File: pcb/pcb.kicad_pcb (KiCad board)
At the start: 2 copper layers, 99.9 x 83.3 mm, 121 parts

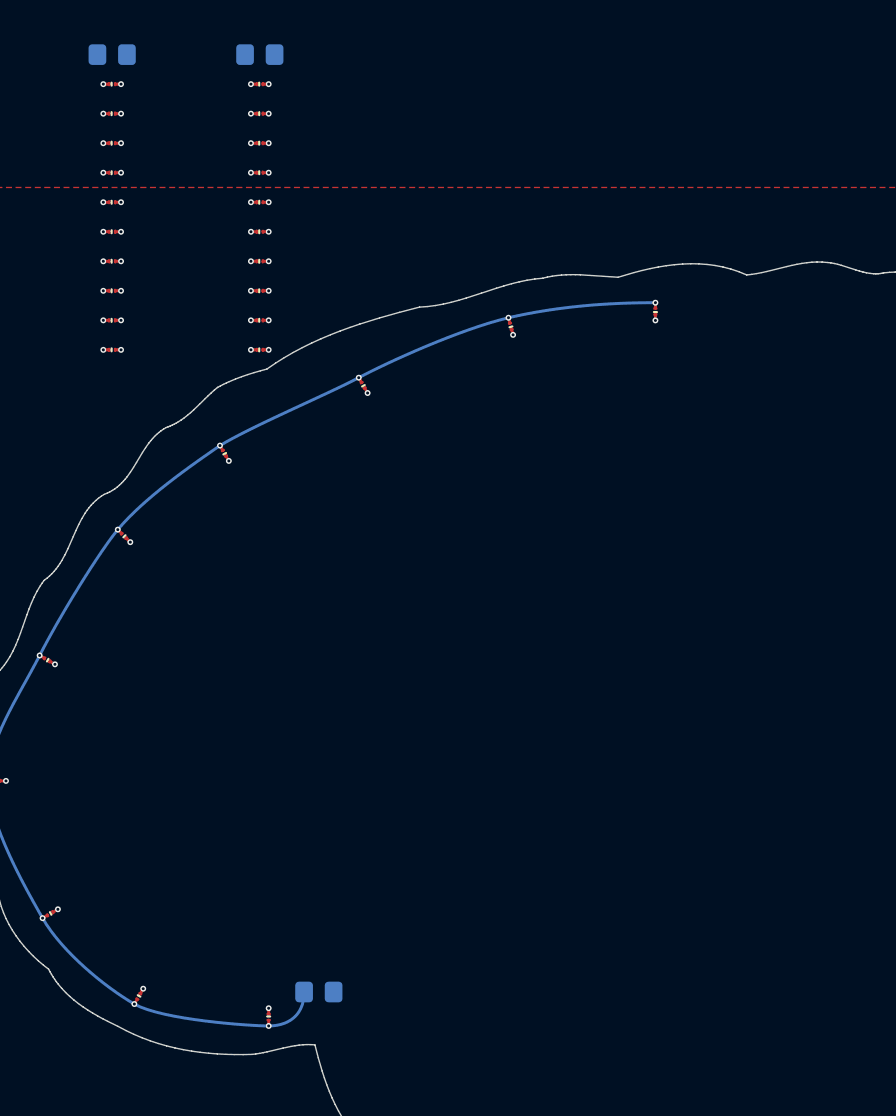
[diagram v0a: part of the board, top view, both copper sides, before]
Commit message: distributed LEDs of frontal cortex and did some experimental wiring for them
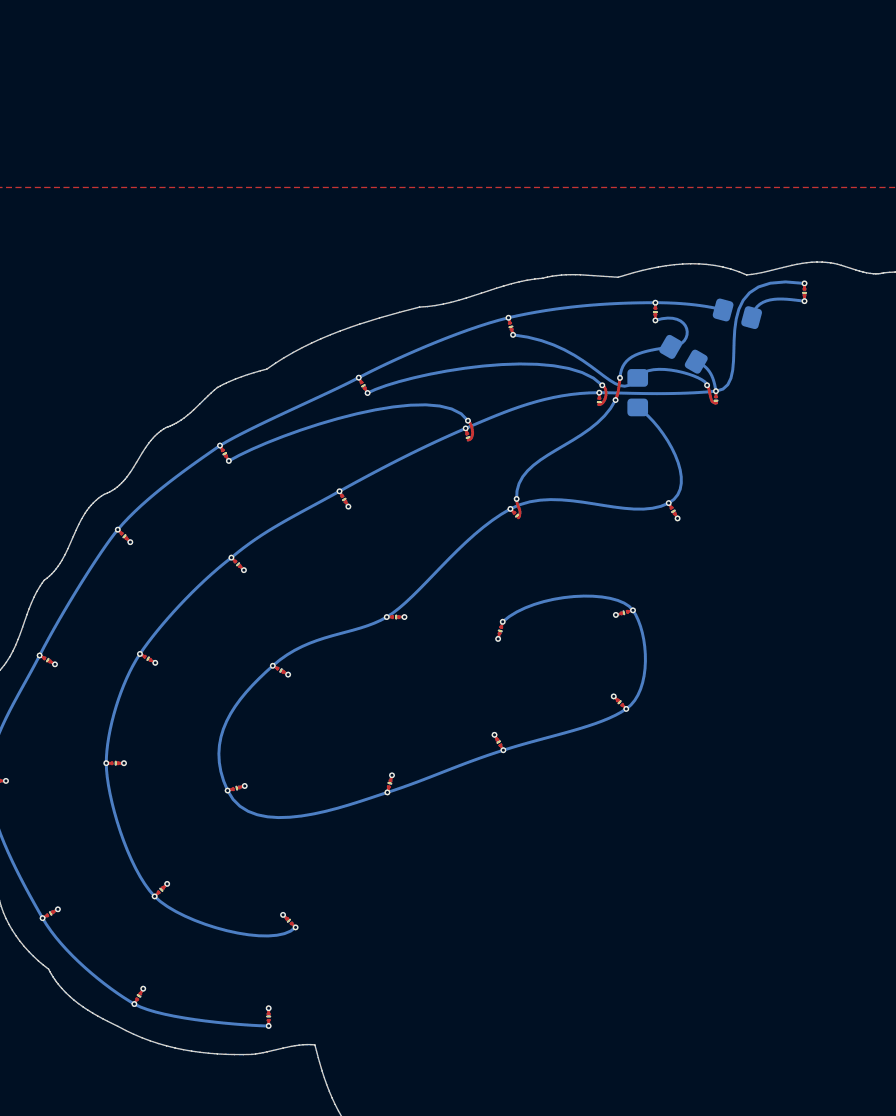
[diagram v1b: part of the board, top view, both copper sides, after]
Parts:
- moved R1 54.0 mm to (152.4, 68.6), turned to -15 degrees
- moved D11 49.0 mm to (156.9, 67.1), turned to 90 degrees
- moved D12 45.3 mm to (150.9, 74.4), turned to 90 degrees
- moved R2 43.7 mm to (148.7, 71.3), turned to 150 degrees
- moved D20 40.5 mm to (122.0, 109.7), turned to -45 degrees
- moved D21 40.2 mm to (148.0, 81.9), turned to 120 degrees
- moved D25 39.7 mm to (118.4, 100.7), turned to -165 degrees
- moved D19 38.7 mm to (113.3, 107.6), turned to -135 degrees
- moved D26 38.4 mm to (128.8, 100.4), turned to -105 degrees
- moved D13 37.4 mm to (143.0, 74.5), turned to 90 degrees
- moved D28 37.1 mm to (144.4, 94.9), turned to -45 degrees
- moved D27 36.4 mm to (136.2, 97.6), turned to -60 degrees
- moved R3 34.3 mm to (145.6, 73.9), turned to 90 degrees
- moved D24 33.7 mm to (121.4, 92.7), turned to 150 degrees
- moved D23 33.4 mm to (129.2, 89.1), turned to 180 degrees
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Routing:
- net /Row1: track 3.95 -> 3.55 mm, vias 10 -> 12

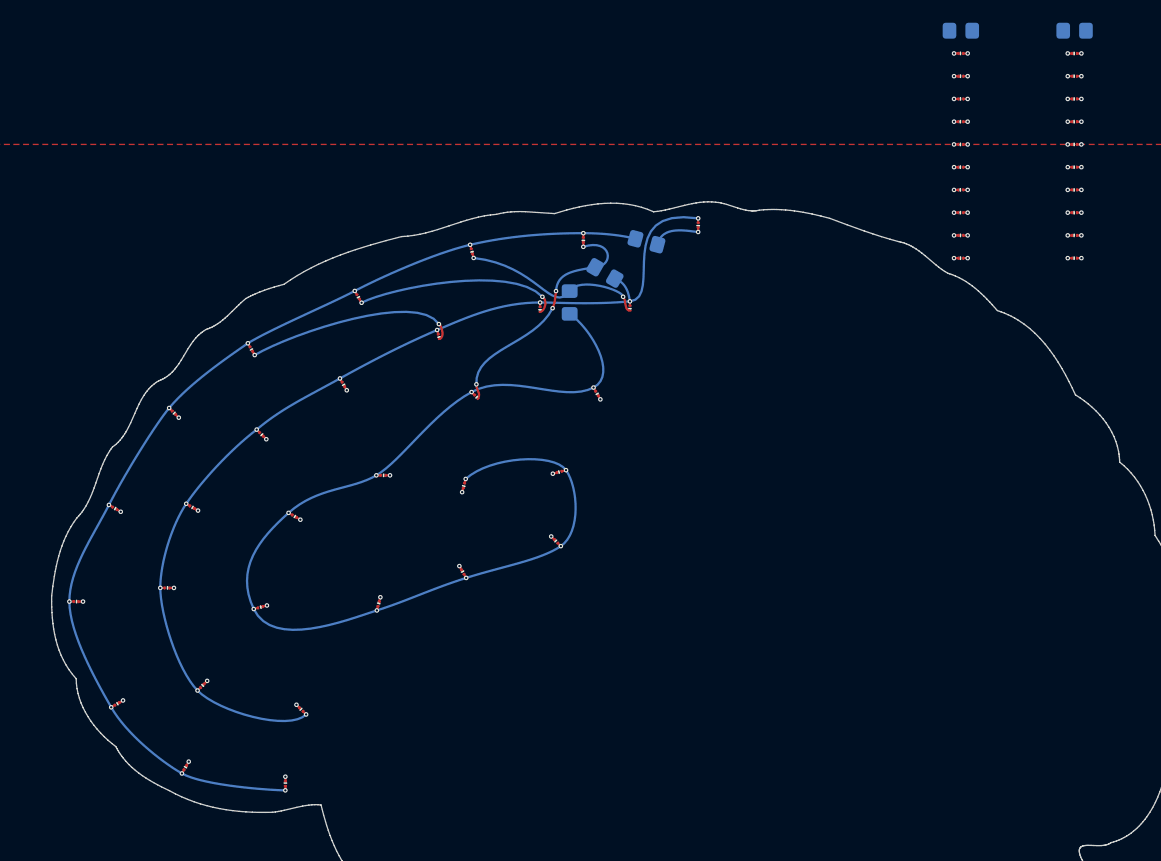
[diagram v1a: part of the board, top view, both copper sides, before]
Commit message: distributed LEDs of parietal lobe (Col3, Col4)
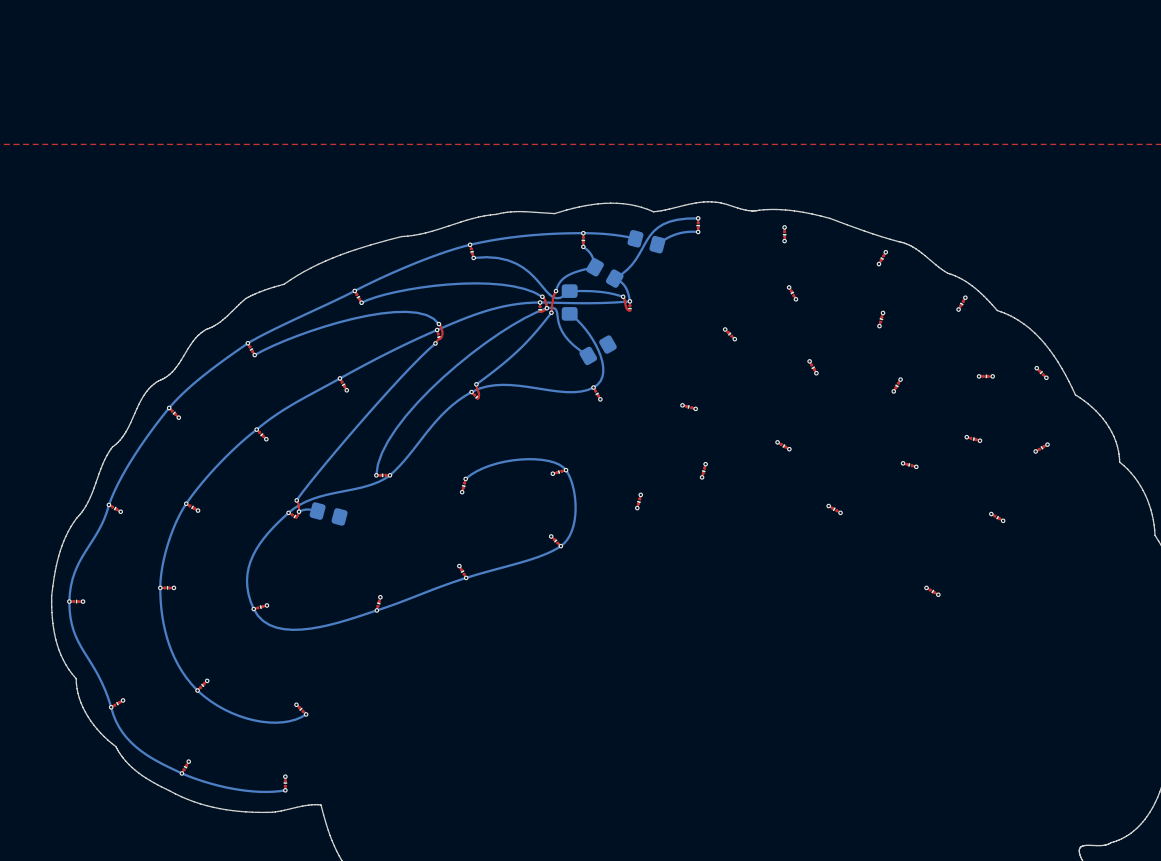
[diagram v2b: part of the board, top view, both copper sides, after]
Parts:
- moved R5 78.2 mm to (124.4, 92.5), turned to 165 degrees
- moved D41 43.0 mm to (164.4, 86.5), turned to 150 degrees
- moved R4 42.5 mm to (148.1, 78.1), turned to -150 degrees
- moved D46 39.3 mm to (177.5, 99.3), turned to 150 degrees
- moved D45 38.4 mm to (168.9, 92.1), turned to -30 degrees
- moved D39 36.7 mm to (151.7, 91.4), turned to 75 degrees
- moved D42 34.4 mm to (167.0, 79.6), turned to 120 degrees
- moved D44 33.5 mm to (175.5, 88.2), turned to -15 degrees
- moved D43 29.6 mm to (174.4, 81.2), turned to 60 degrees
- moved D47 29.6 mm to (183.2, 92.8), turned to 150 degrees
- moved D38 29.4 mm to (156.1, 83.1), turned to -15 degrees
- moved D40 29.3 mm to (157.4, 88.7), turned to 75 degrees
- moved D37 23.9 mm to (159.7, 76.7), turned to -45 degrees
- moved D34 23.2 mm to (187.1, 80.1), turned to -45 degrees
- moved D31 22.2 mm to (164.5, 67.9), turned to 90 degrees
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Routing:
- net /Row4: track 3.55 -> 3.16 mm, vias 10 -> 12
- net /Row3: vias 10 -> 11

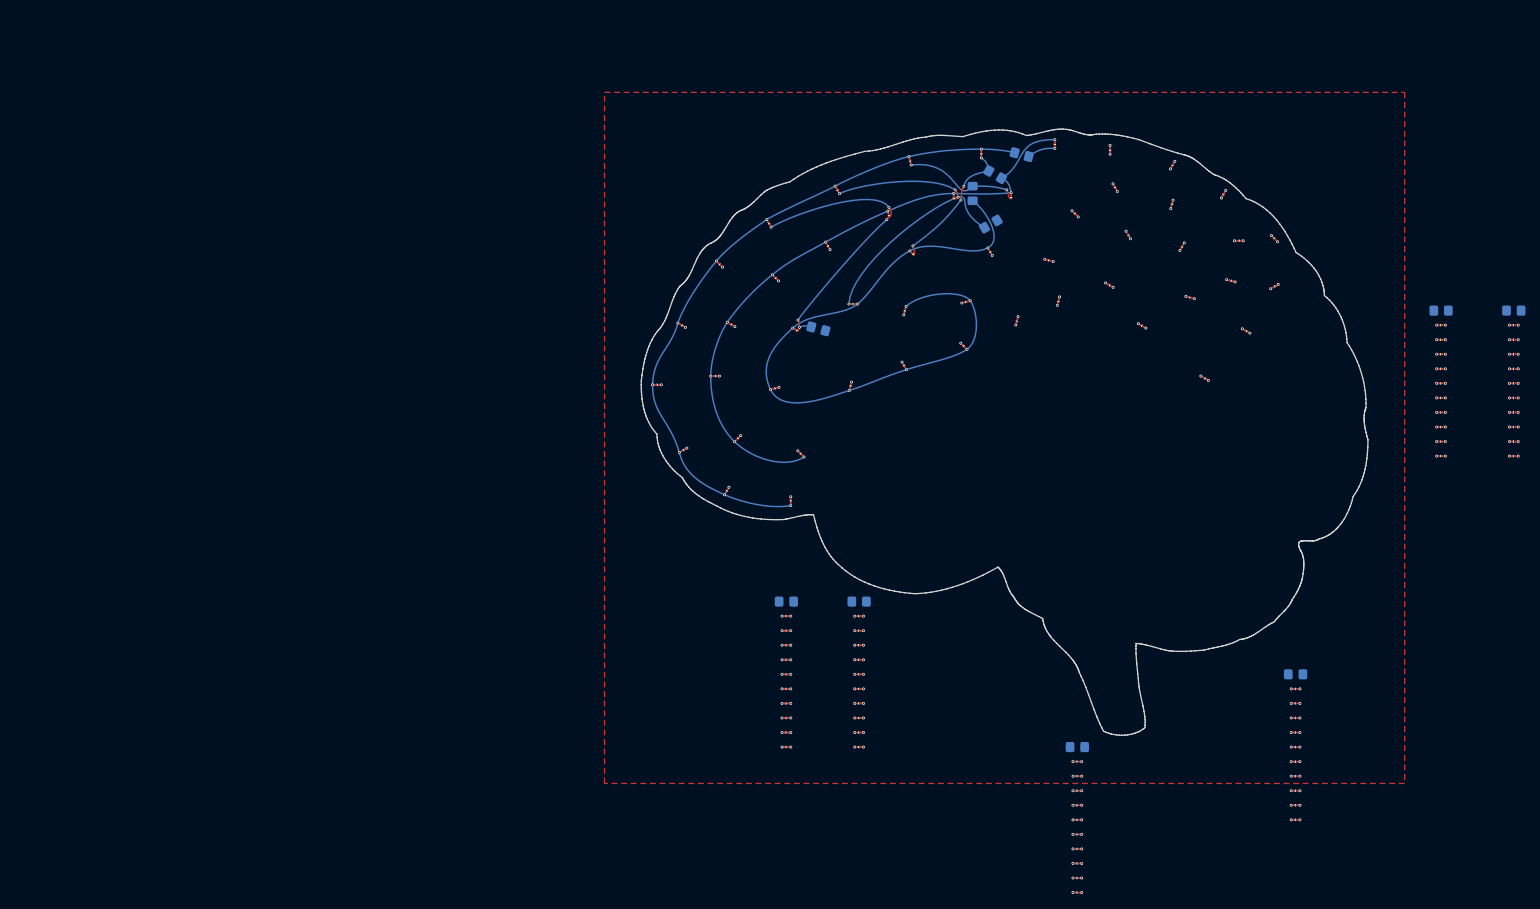
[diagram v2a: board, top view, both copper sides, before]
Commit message: added attachement points for necklace and worked on LED placement and wiring drafted concept for organizing the matrix wiring added buttons and ESP32 module to PCB started laying out the LED positions and wire paths with points and lines on User layers (User.1: LED positions, User.2: Resistor positions, User.3: Row paths, User.4: Column paths)
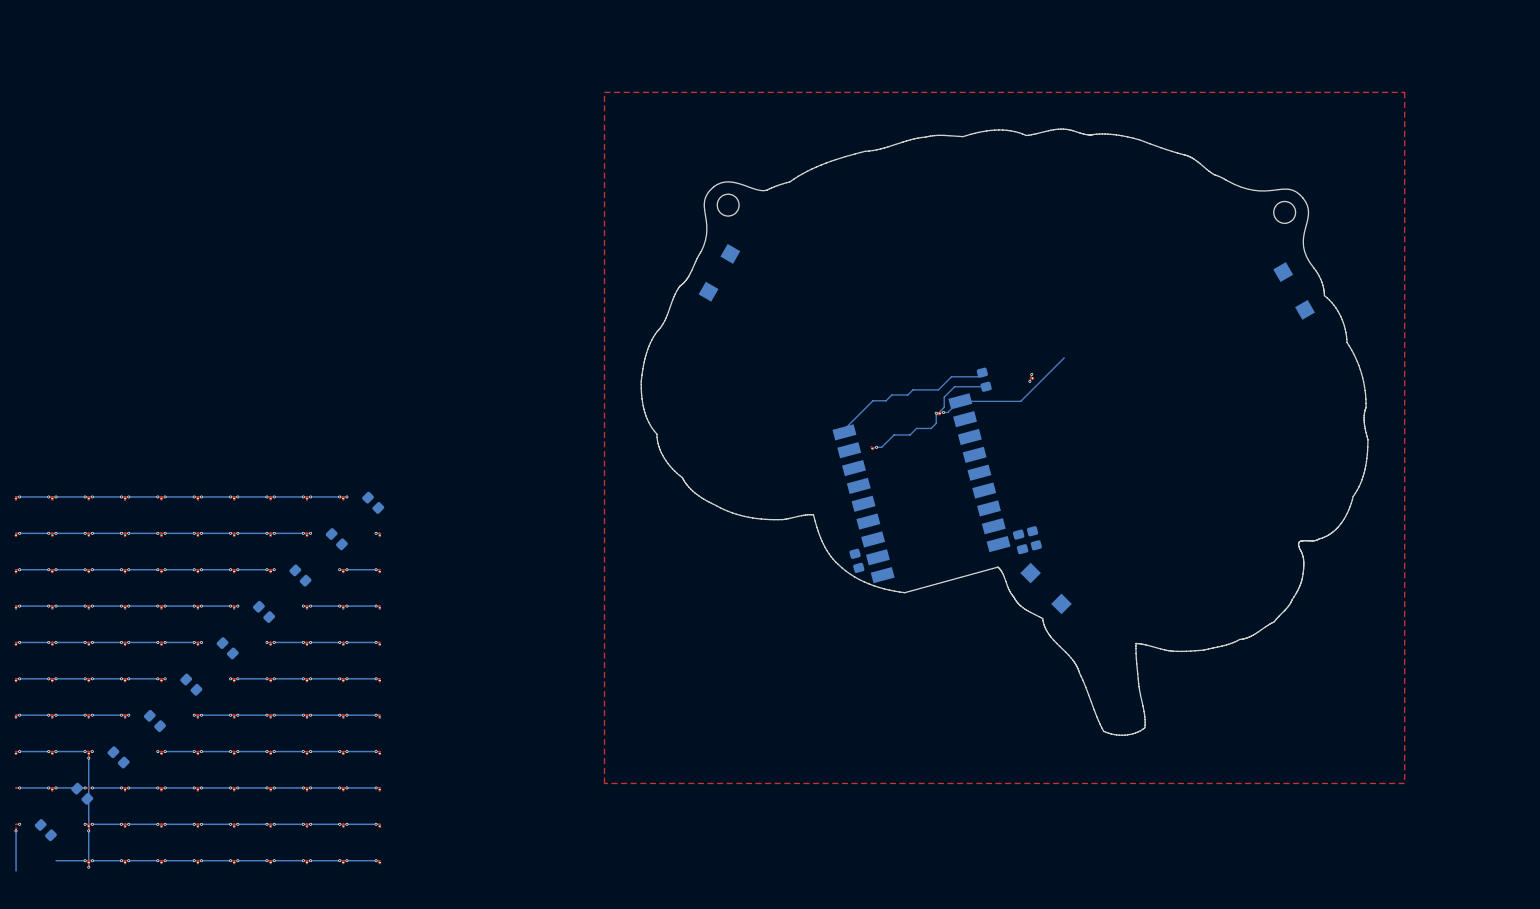
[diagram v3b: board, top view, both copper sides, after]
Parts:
- added C1: 100n, Capacitor_SMD:C_0805_2012Metric_Pad1.18x1.45mm_HandSolder, B.Cu at (152.2, 121.8)
- added R12: 10k, Resistor_SMD:R_0805_2012Metric_Pad1.20x1.40mm_HandSolder, B.Cu at (129.7, 124.4)
- added R13: 2k2, Resistor_SMD:R_0805_2012Metric_Pad1.20x1.40mm_HandSolder, B.Cu at (154.1, 121.3)
- added SW1: SW_Push, pcb:SW_Push_1P1T_NO_Alps_SPEH, B.Cu at (110.8, 84.8)
- added SW2: SW_Push, pcb:SW_Push_1P1T_NO_Alps_SPEH, B.Cu at (189.8, 87.3)
- added SW3: SW_Push, pcb:SW_Push_1P1T_NO_Alps_SPEH, B.Cu at (155.7, 128.2)
- added U1: ~, Waveshare-ESP32:Waveshare-ESP32-Cx-Zero, B.Cu at (138.2, 114.8)
- moved D81 208.7 mm to (14.1, 125.8), turned to 90 degrees
- moved D82 203.4 mm to (19.1, 125.8), turned to 90 degrees
- moved D71 199.7 mm to (14.1, 130.8), turned to 90 degrees
- moved D83 198.2 mm to (24.1, 125.8), turned to 90 degrees
- moved D72 194.4 mm to (19.1, 130.8), turned to 90 degrees
- moved D84 192.9 mm to (29.1, 125.8), turned to 90 degrees
- moved D73 189.1 mm to (24.1, 130.8), turned to 90 degrees
- moved D85 187.7 mm to (34.1, 125.8), turned to 90 degrees
- moved D74 183.9 mm to (29.1, 130.8), turned to 90 degrees
- moved D86 182.5 mm to (39.1, 125.8), turned to 90 degrees
- moved D75 178.6 mm to (34.1, 130.8), turned to 90 degrees
- moved D101 177.8 mm to (14.1, 115.8), turned to 90 degrees
- moved D87 177.2 mm to (44.1, 125.8), turned to 90 degrees
- moved D32 173.9 mm to (19.1, 150.8), turned to 90 degrees
- moved D33 173.9 mm to (24.1, 150.8), turned to 90 degrees
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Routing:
- net /Col0: track 3.95 -> 68.1 mm, vias 10 -> 19
- net /Col1: track 3.95 -> 61.2 mm, vias 10 -> 19
- net /Col2: track 3.95 -> 50.1 mm, vias 10 -> 20
- net /Col10: track 3.95 -> 45.5 mm, vias 10 -> 19
- net /Col4: track 3.95 -> 41.0 mm, vias 10 -> 18
- net /Col3: track 3.95 -> 41.0 mm, vias 10 -> 18
- net /Col8: track 3.95 -> 41.0 mm, vias 10 -> 18
- net /Col6: track 3.95 -> 41.0 mm, vias 10 -> 18
- net /Col7: track 3.95 -> 41.0 mm, vias 10 -> 18
- net /Col5: track 3.95 -> 41.0 mm, vias 10 -> 18
- net /Col9: track 3.95 -> 41.0 mm, vias 10 -> 18
- net /Row0: track 3.95 -> 27.3 mm, vias 10 -> 3
- net /Row2: track 3.55 -> 16.6 mm, vias 10 -> 3
- net /Row7: track 3.95 -> 0.00 mm, vias 10 -> 0
- net /Row8: track 3.95 -> 0.00 mm, vias 10 -> 0
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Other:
- outline, holes or cut-outs redrawn
- board text added: "Col0"
- board text added: "Col1"
- board text added: "Col10"
- board text added: "Col2"
- board text added: "Col3"
- board text added: "Col4"
- board text added: "Col5"
- board text added: "Col6"
- board text added: "Col7"
- board text added: "Col8"
- board text added: "Col9"
- board text added: "Row0"
- board text added: "Row1"
